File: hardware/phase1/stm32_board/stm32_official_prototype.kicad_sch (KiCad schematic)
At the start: 74 parts, among them CN11 Conn_02x36_Odd_Even, CN12 Conn_02x36_Odd_Even, CN14 USB_B_Micro, CN5 Conn_ARM_JTAG_SWD_10, T2 9013, U11 STM32L496ZGTx, U12 STMPS2151STR, U13 USBLC6-2SC6, U6 LD39050PU33R, U8 TSV631AILT, U9 ESDALC6V1W5

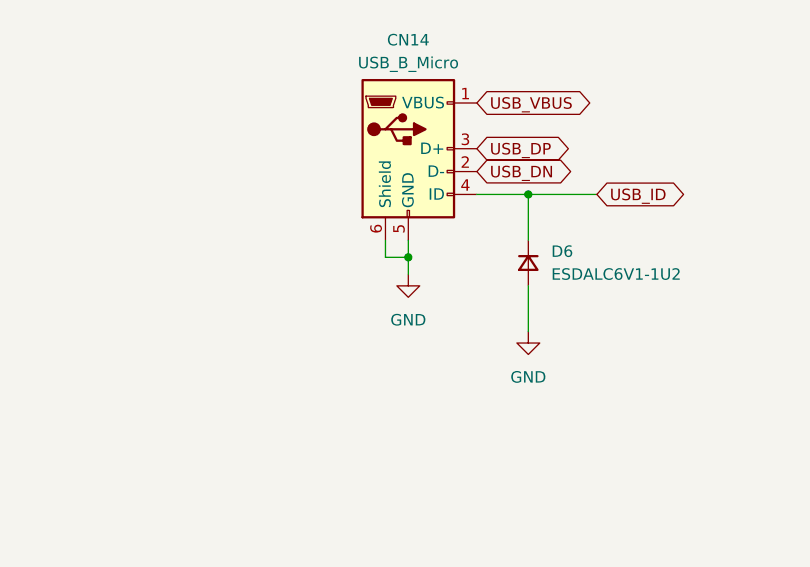
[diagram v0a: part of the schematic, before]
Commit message: Update STM32 to unconnect uUSB shield from GND
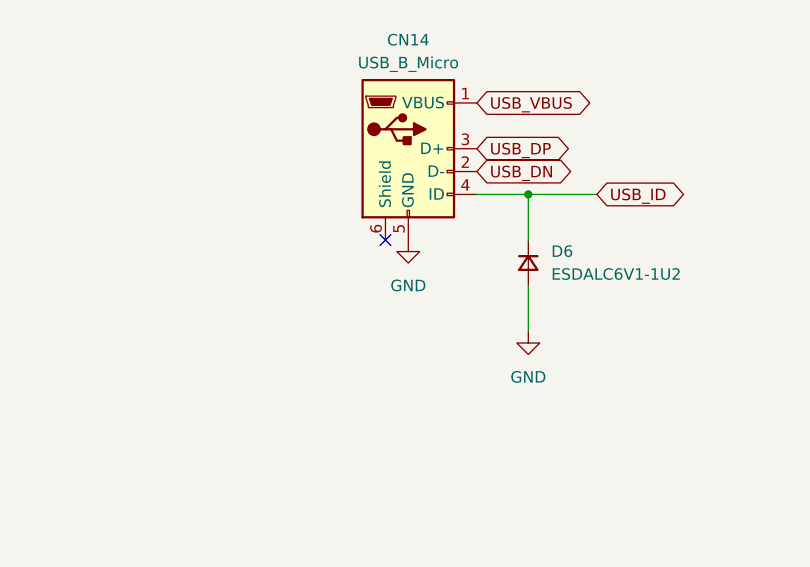
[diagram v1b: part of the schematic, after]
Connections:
- net GND: no longer CN14.6 (Shield)
- no-connect marks 6 -> 7
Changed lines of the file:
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@@
 	)
 	(junction
-		(at 581.66 51.435)
-		(diameter 0)
-		(color 0 0 0 0)
-	)
-	(junction
 		(at 796.925 55.88)
 		(diameter 0)
@@
 		(at 263.525 189.865)
 	)
+	(no_connect
+		(at 579.12 49.53)
+	)
 	(wire
 		(pts
@@
 	(wire
 		(pts
-			(xy 581.66 53.34) (xy 581.66 51.435)
-		)
-		(stroke
-			(width 0)
-			(type default)
-		)
-	)
-	(wire
-		(pts
 			(xy 142.875 92.71) (xy 127.635 92.71)
 		)
@@
 	(wire
 		(pts
-			(xy 579.12 51.435) (xy 581.66 51.435)
-		)
-		(stroke
-			(width 0)
-			(type default)
-		)
-	)
-	(wire
-		(pts
 			(xy 102.235 54.61) (xy 102.235 52.07)
 		)
@@
 	(wire
 		(pts
-			(xy 579.12 49.53) (xy 579.12 51.435)
-		)
-		(stroke
-			(width 0)
-			(type default)
-		)
-	)
-	(wire
-		(pts
 			(xy 142.875 97.79) (xy 127.635 97.79)
 		)
@@
 	(wire
 		(pts
-			(xy 581.66 51.435) (xy 581.66 49.53)
-		)
-		(stroke
-			(width 0)
-			(type default)
-		)
-	)
-	(wire
-		(pts
 			(xy 253.365 62.23) (xy 264.16 62.23)
 		)
@@
 	(label "Diff Pair (+) 90ohm"
 		(at 491.49 71.755 0)
+		(fields_autoplaced yes)
 		(effects
 			(font
@@
 	(label "Diff Pair (-) 90ohm"
 		(at 491.49 61.595 0)
+		(fields_autoplaced yes)
 		(effects
 			(font
@@
 	(symbol
 		(lib_id "power:GND")
-		(at 581.66 53.34 0)
-		(unit 1)
-		(exclude_from_sim no)
-		(in_bom yes)
-		(on_board yes)
-		(dnp no)
-		(fields_autoplaced yes)
-		(property "Reference" "#PWR048"
-			(at 581.66 59.69 0)
-			(effects
-				(font
-					(size 1.27 1.27)
-				)
-				(hide yes)
-			)
-		)
-		(property "Value" "GND"
-			(at 581.66 58.42 0)
-			(effects
-				(font
-					(size 1.27 1.27)
-				)
-			)
-		)
-		(property "Footprint" ""
-			(at 581.66 53.34 0)
-			(effects
-				(font
-					(size 1.27 1.27)
-				)
-				(hide yes)
-			)
-		)
-		(property "Datasheet" ""
-			(at 581.66 53.34 0)
-			(effects
-				(font
-					(size 1.27 1.27)
-				)
-				(hide yes)
-			)
-		)
-		(property "Description" "Power symbol creates a global label with name \"GND\" , ground"
-			(at 581.66 53.34 0)
-			(effects
-				(font
-					(size 1.27 1.27)
-				)
-				(hide yes)
-			)
-		)
-		(pin "1"
-		)
-		(instances
-			(project "stm32_official_prototype"
-				(path "/eb5365fc-f6b5-4558-a59a-9210174c0865"
-					(reference "#PWR048")
-					(unit 1)
-				)
-			)
-		)
-	)
-	(symbol
-		(lib_id "power:GND")
 		(at 727.71 97.155 90)
 		(unit 1)
@@
 					(unit 1)
 				)
+			)
+		)
+	)
+	(symbol
+		(lib_id "power:GND")
+		(at 581.66 49.53 0)
+		(unit 1)
+		(exclude_from_sim no)
+		(in_bom yes)
+		(on_board yes)
+		(dnp no)
+		(fields_autoplaced yes)
+		(property "Reference" "#PWR06"
+			(at 581.66 55.88 0)
+			(effects
+				(font
+					(size 1.27 1.27)
+				)
+				(hide yes)
+			)
+		)
+		(property "Value" "GND"
+			(at 581.66 54.61 0)
+			(effects
+				(font
+					(size 1.27 1.27)
+				)
+			)
+		)
+		(property "Footprint" ""
+			(at 581.66 49.53 0)
+			(effects
+				(font
+					(size 1.27 1.27)
+				)
+				(hide yes)
+			)
+		)
+		(property "Datasheet" ""
+			(at 581.66 49.53 0)
+			(effects
+				(font
+					(size 1.27 1.27)
+				)
+				(hide yes)
+			)
+		)
+		(property "Description" "Power symbol creates a global label with name \"GND\" , ground"
+			(at 581.66 49.53 0)
+			(effects
+				(font
+					(size 1.27 1.27)
+				)
+				(hide yes)
+			)
+		)
+		(pin "1"
+		)
+		(instances
+			(project "stm32_official_prototype"
+				(path "/eb5365fc-f6b5-4558-a59a-9210174c0865"
+					(reference "#PWR06")
+					(unit 1)
+				)

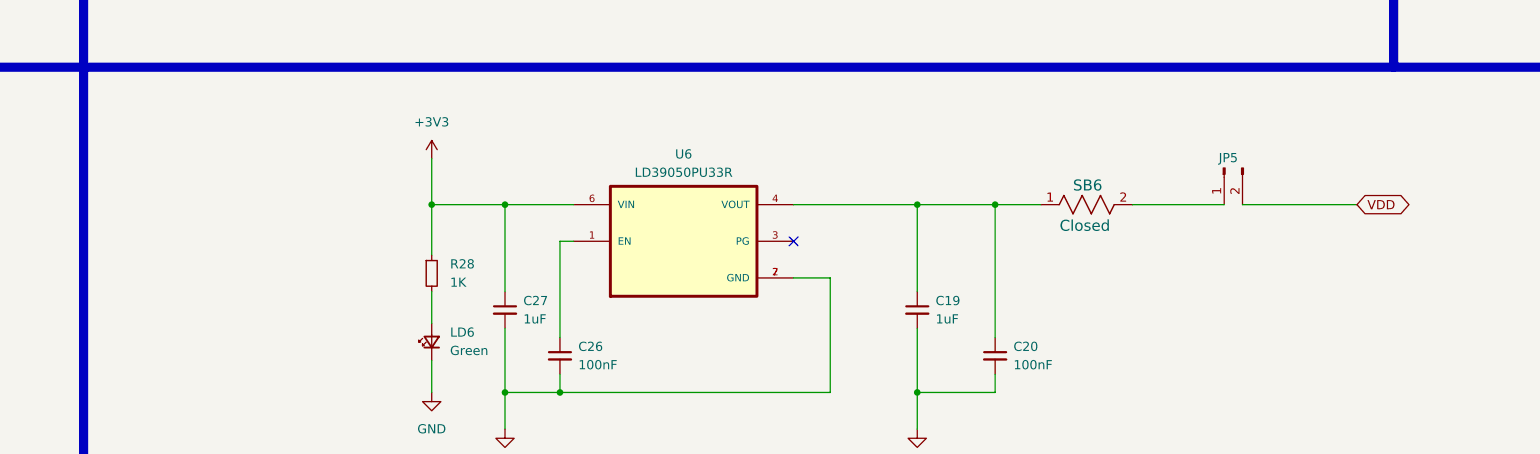
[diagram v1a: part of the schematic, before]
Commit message: revised final stm32 prototype (2.19.25)
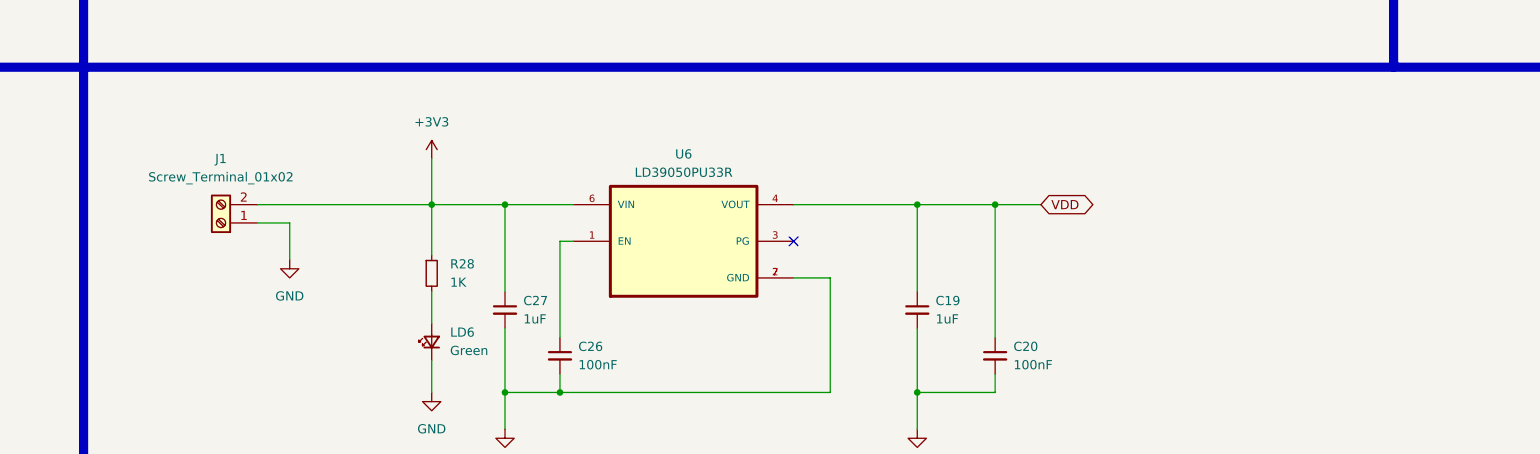
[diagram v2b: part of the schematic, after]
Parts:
- removed JP5: Conn_01x02_Pin, Connector_PinHeader_2.54mm:PinHeader_1x02_P2.54mm_Vertical, symbol Connector:Conn_01x02_Pin
- removed SB6: Closed, RC0603JR-070RL:RESC1607X60N, symbol RC0603JR-070RL:RC0603JR-070RL
- added J1: Screw_Terminal_01x02, 1725656:PHOENIX_1725656, symbol Connector:Screw_Terminal_01x02
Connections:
- net +3V3: now also J1.2 (Pin_2)
- net GND: now also J1.1 (Pin_1)
- net VDD: now also C19.1, C20.1, U6.4 (VOUT)
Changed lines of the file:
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@@
 	(wire
 		(pts
+			(xy 476.885 302.26) (xy 472.44 302.26)
+		)
+		(stroke
+			(width 0)
+			(type default)
+		)
+	)
+	(wire
+		(pts
 			(xy 263.525 194.945) (xy 279.4 194.945)
 		)
@@
 	(wire
 		(pts
-			(xy 593.725 299.72) (xy 606.425 299.72)
-		)
-		(stroke
-			(width 0)
-			(type default)
-		)
-	)
-	(wire
-		(pts
 			(xy 370.84 85.09) (xy 391.16 85.09)
 		)
@@
 	(wire
 		(pts
+			(xy 476.885 307.34) (xy 476.885 302.26)
+		)
+		(stroke
+			(width 0)
+			(type default)
+		)
+	)
+	(wire
+		(pts
 			(xy 81.915 52.07) (xy 81.915 54.61)
 		)
@@
 	(wire
 		(pts
+			(xy 472.44 299.72) (xy 496.57 299.72)
+		)
+		(stroke
+			(width 0)
+			(type default)
+		)
+	)
+	(wire
+		(pts
 			(xy 153.035 123.19) (xy 155.575 123.19)
 		)
@@
 	(wire
 		(pts
-			(xy 608.965 299.72) (xy 624.84 299.72)
-		)
-		(stroke
-			(width 0)
-			(type default)
-		)
-	)
-	(wire
-		(pts
 			(xy 570.23 231.14) (xy 560.07 231.14)
 		)
@@
 	(label "Diff Pair (+) 90ohm"
 		(at 491.49 71.755 0)
-		(fields_autoplaced yes)
 		(effects
 			(font
@@
 	(label "Diff Pair (-) 90ohm"
 		(at 491.49 61.595 0)
-		(fields_autoplaced yes)
 		(effects
 			(font
@@
 	(global_label "VDD"
 		(shape bidirectional)
-		(at 624.84 299.72 0)
+		(at 581.025 299.72 0)
 		(fields_autoplaced yes)
 		(effects
@@
 		)
 		(property "Intersheetrefs" "${INTERSHEET_REFS}"
-			(at 632.5651 299.72 0)
+			(at 588.7501 299.72 0)
 			(effects
 				(font
@@
 	)
 	(symbol
-		(lib_id "Connector:Conn_01x02_Pin")
-		(at 606.425 294.64 90)
-		(mirror x)
-		(unit 1)
-		(exclude_from_sim no)
-		(in_bom yes)
-		(on_board yes)
-		(dnp no)
-		(property "Reference" "JP5"
-			(at 605.663 293.243 90)
-			(effects
-				(font
-					(size 1.27 1.27)
-				)
-				(justify right)
-			)
-		)
-		(property "Value" "Conn_01x02_Pin"
-			(at 610.87 294.0051 90)
-			(effects
-				(font
-					(size 1.27 1.27)
-				)
-				(justify right)
-				(hide yes)
-			)
-		)
-		(property "Footprint" "Connector_PinHeader_2.54mm:PinHeader_1x02_P2.54mm_Vertical"
-			(at 606.425 294.64 0)
-			(effects
-				(font
-					(size 1.27 1.27)
-				)
-				(hide yes)
-			)
-		)
-		(property "Datasheet" "~"
-			(at 606.425 294.64 0)
-			(effects
-				(font
-					(size 1.27 1.27)
-				)
-				(hide yes)
-			)
-		)
-		(property "Description" "Generic connector, single row, 01x02, script generated"
-			(at 606.425 294.64 0)
-			(effects
-				(font
-					(size 1.27 1.27)
-				)
-				(hide yes)
-			)
-		)
-		(pin "2"
-		)
-		(pin "1"
-		)
-		(instances
-			(project "stm32_official_prototype"
-				(path "/eb5365fc-f6b5-4558-a59a-9210174c0865"
-					(reference "JP5")
-					(unit 1)
-				)
-			)
-		)
-	)
-	(symbol
 		(lib_id "Device:R_Small")
 		(at 679.45 215.265 90)
@@
 	)
 	(symbol
+		(lib_id "power:GND")
+		(at 476.885 307.34 0)
+		(unit 1)
+		(exclude_from_sim no)
+		(in_bom yes)
+		(on_board yes)
+		(dnp no)
+		(fields_autoplaced yes)
+		(property "Reference" "#PWR07"
+			(at 476.885 313.69 0)
+			(effects
+				(font
+					(size 1.27 1.27)
+				)
+				(hide yes)
+			)
+		)
+		(property "Value" "GND"
+			(at 476.885 312.42 0)
+			(effects
+				(font
+					(size 1.27 1.27)
+				)
+			)
+		)
+		(property "Footprint" ""
+			(at 476.885 307.34 0)
+			(effects
+				(font
+					(size 1.27 1.27)
+				)
+				(hide yes)
+			)
+		)
+		(property "Datasheet" ""
+			(at 476.885 307.34 0)
+			(effects
+				(font
+					(size 1.27 1.27)
+				)
+				(hide yes)
+			)
+		)
+		(property "Description" "Power symbol creates a global label with name \"GND\" , ground"
+			(at 476.885 307.34 0)
+			(effects
+				(font
+					(size 1.27 1.27)
+				)
+				(hide yes)
+			)
+		)
+		(pin "1"
+		)
+		(instances
+			(project "stm32_official_prototype"
+				(path "/eb5365fc-f6b5-4558-a59a-9210174c0865"
+					(reference "#PWR07")
+					(unit 1)
+				)
+			)
+		)
+	)
+	(symbol
 		(lib_id "RC0603JR-070RL:RC0603JR-070RL")
 		(at 140.335 123.19 0)
@@
 	)
 	(symbol
-		(lib_id "RC0603JR-070RL:RC0603JR-070RL")
-		(at 581.025 299.72 0)
-		(unit 1)
-		(exclude_from_sim no)
-		(in_bom yes)
-		(on_board yes)
-		(dnp no)
-		(property "Reference" "SB6"
-			(at 587.502 297.053 0)
-			(effects
-				(font
-					(size 1.524 1.524)
-				)
-			)
-		)
-		(property "Value" "Closed"
-			(at 587.121 302.641 0)
-			(effects
-				(font
-					(size 1.524 1.524)
-				)
-			)
-		)
-		(property "Footprint" "RC0603JR-070RL:RESC1607X60N"
-			(at 581.025 299.72 0)
-			(effects
-				(font
-					(size 1.27 1.27)
-					(italic yes)
-				)
-				(hide yes)
-			)
-		)
-		(property "Datasheet" "RC0603JR-070RL"
-			(at 581.025 299.72 0)
-			(effects
-				(font
-					(size 1.27 1.27)
-					(italic yes)
-				)
-				(hide yes)
-			)
-		)
-		(property "Description" ""
-			(at 581.025 299.72 0)
-			(effects
-				(font
-					(size 1.27 1.27)
-				)
-				(hide yes)
-			)
-		)
-		(pin "1"
-		)
-		(pin "2"
-		)
-		(instances
-			(project "stm32_official_prototype"
-				(path "/eb5365fc-f6b5-4558-a59a-9210174c0865"
-					(reference "SB6")
-					(unit 1)
-				)
-			)
-		)
-	)
-	(symbol
 		(lib_id "LD39050PU33R:LD39050PU33R")
 		(at 531.495 304.8 0)
@@
 					(unit 1)
 				)
+			)
+		)
+	)
+	(symbol
+		(lib_id "Connector:Screw_Terminal_01x02")
+		(at 467.36 302.26 180)
+		(unit 1)
+		(exclude_from_sim no)
+		(in_bom yes)
+		(on_board yes)
+		(dnp no)
+		(fields_autoplaced yes)
+		(property "Reference" "J1"
+			(at 467.36 293.37 0)
+			(effects
+				(font
+					(size 1.27 1.27)
+				)
+			)
+		)
+		(property "Value" "Screw_Terminal_01x02"
+			(at 467.36 295.91 0)
+			(effects
+				(font
+					(size 1.27 1.27)
+				)
+			)
+		)
+		(property "Footprint" "1725656:PHOENIX_1725656"
+			(at 467.36 302.26 0)
+			(effects
+				(font
+					(size 1.27 1.27)
+				)
+				(hide yes)
+			)
+		)
+		(property "Datasheet" "~"
+			(at 467.36 302.26 0)
+			(effects
+				(font
+					(size 1.27 1.27)
+				)
+				(hide yes)
+			)
+		)
+		(property "Description" "Generic screw terminal, single row, 01x02, script generated (kicad-library-utils/schlib/autogen/connector/)"
+			(at 467.36 302.26 0)
+			(effects
+				(font
+					(size 1.27 1.27)
+				)
+				(hide yes)
+			)
+		)
+		(pin "1"
+		)
+		(pin "2"
+		)
+		(instances
+			(project ""
+				(path "/eb5365fc-f6b5-4558-a59a-9210174c0865"
+					(reference "J1")
+					(unit 1)
+				)
